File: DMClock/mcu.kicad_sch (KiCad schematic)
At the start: 31 parts, among them J7 Conn_01x02_Pin, J9 Conn_01x02_Pin, Q1 2SC1815, Q2 2SC1815, SW1 SW_Push, SW10 SW_Push, SW3 SW_SP3T (mode select), SW7 SW_Push, SW8 SW_Push, SW9 SW_Push, U1 PIC16F18346-P, U2 DS3231SN_

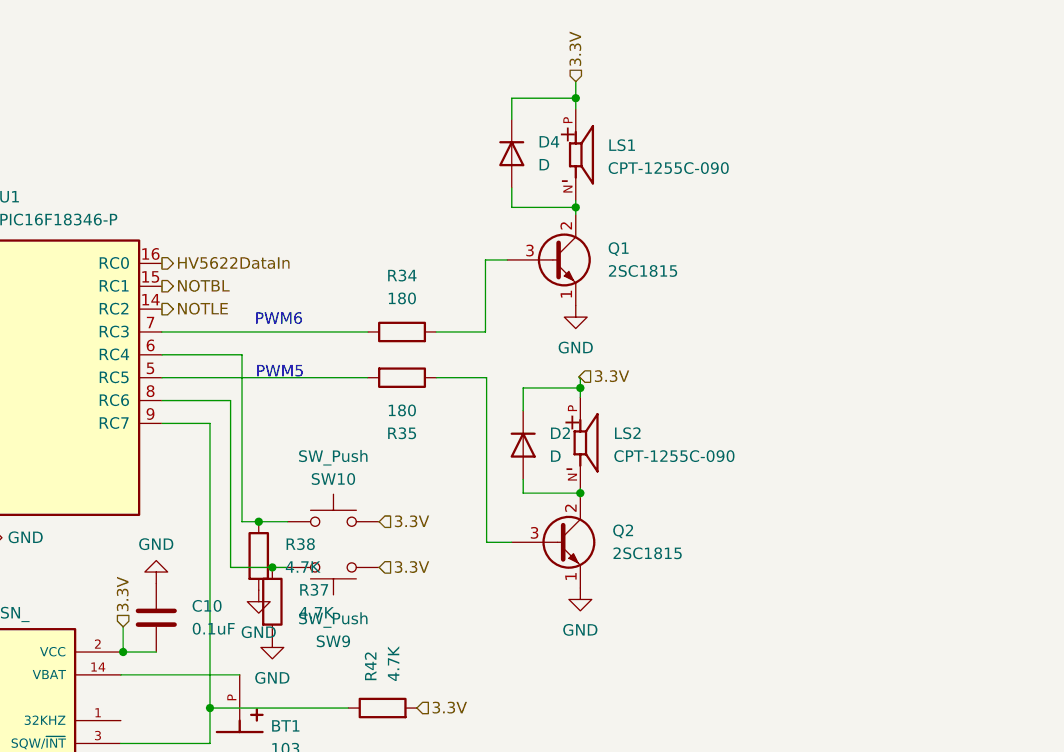
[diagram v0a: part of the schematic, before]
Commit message: need to add timer6 implementation
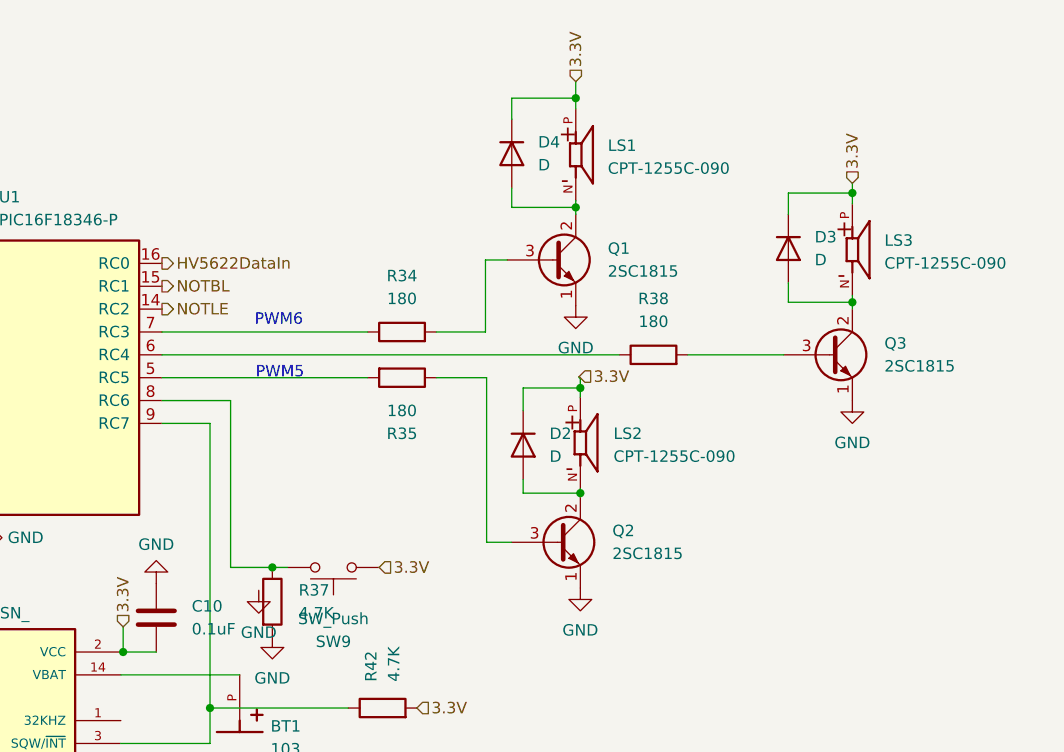
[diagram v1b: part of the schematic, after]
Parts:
- removed SW10: SW_Push, Connector_PinHeader_2.54mm:PinHeader_1x02_P2.54mm_Vertical, symbol Switch:SW_Push
- added D3: D, Diode_THT:D_A-405_P2.54mm_Vertical_AnodeUp, symbol Device:D
- added LS3: CPT-1255C-090, Footprints:CUI_CPT-1255C-090, symbol CPT-1255C-090:CPT-1255C-090
- added Q3: 2SC1815, Package_TO_SOT_THT:TO-92_Inline, symbol Transistor_BJT:2SC1815
- R38: value 4.7K -> 180
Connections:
- net 3.3V: now also D3.1 (K), LS3.P
- net GND: now also Q3.1 (E); no longer R38.2
- new net: D3.2 (A), LS3.N, Q3.2 (C)
- new net: Q3.3 (B), R38.2

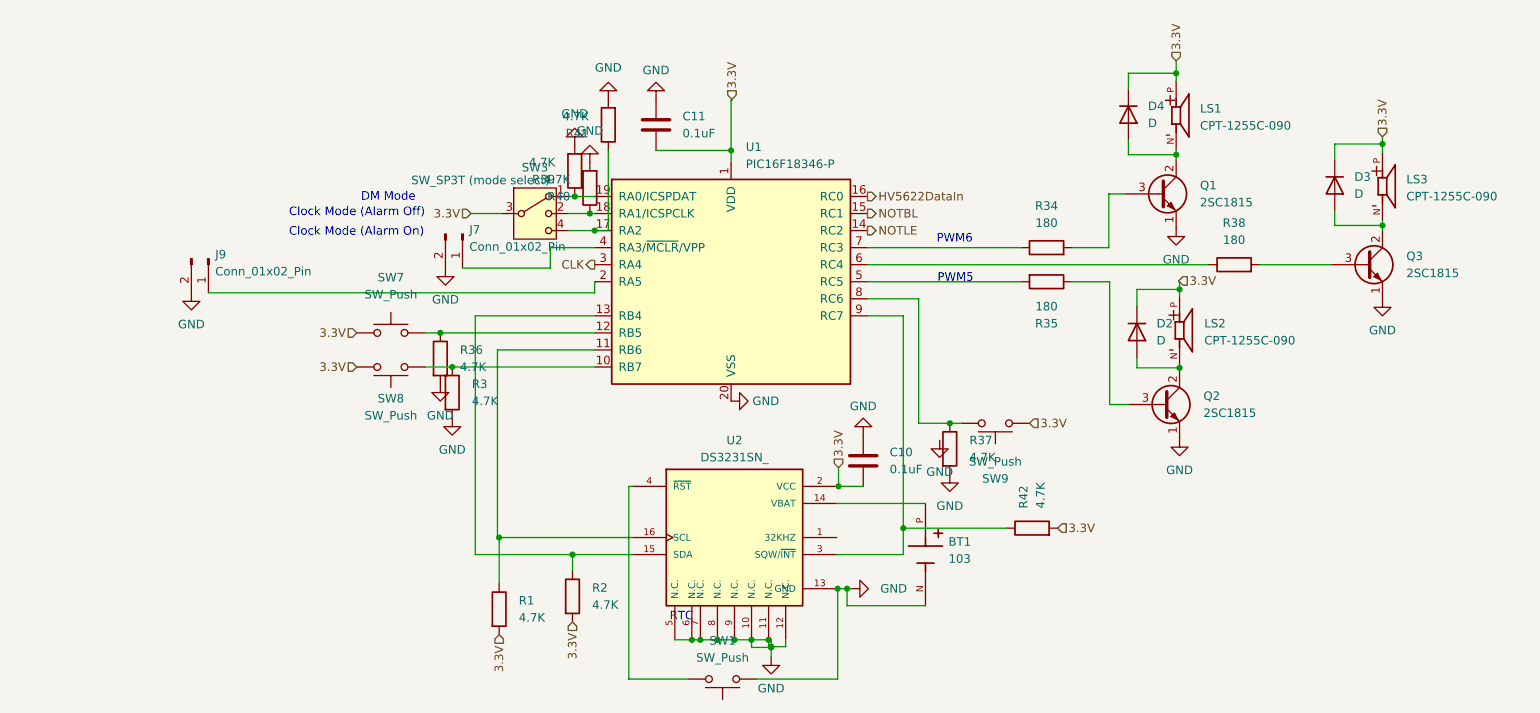
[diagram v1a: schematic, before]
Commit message: updated buck converter
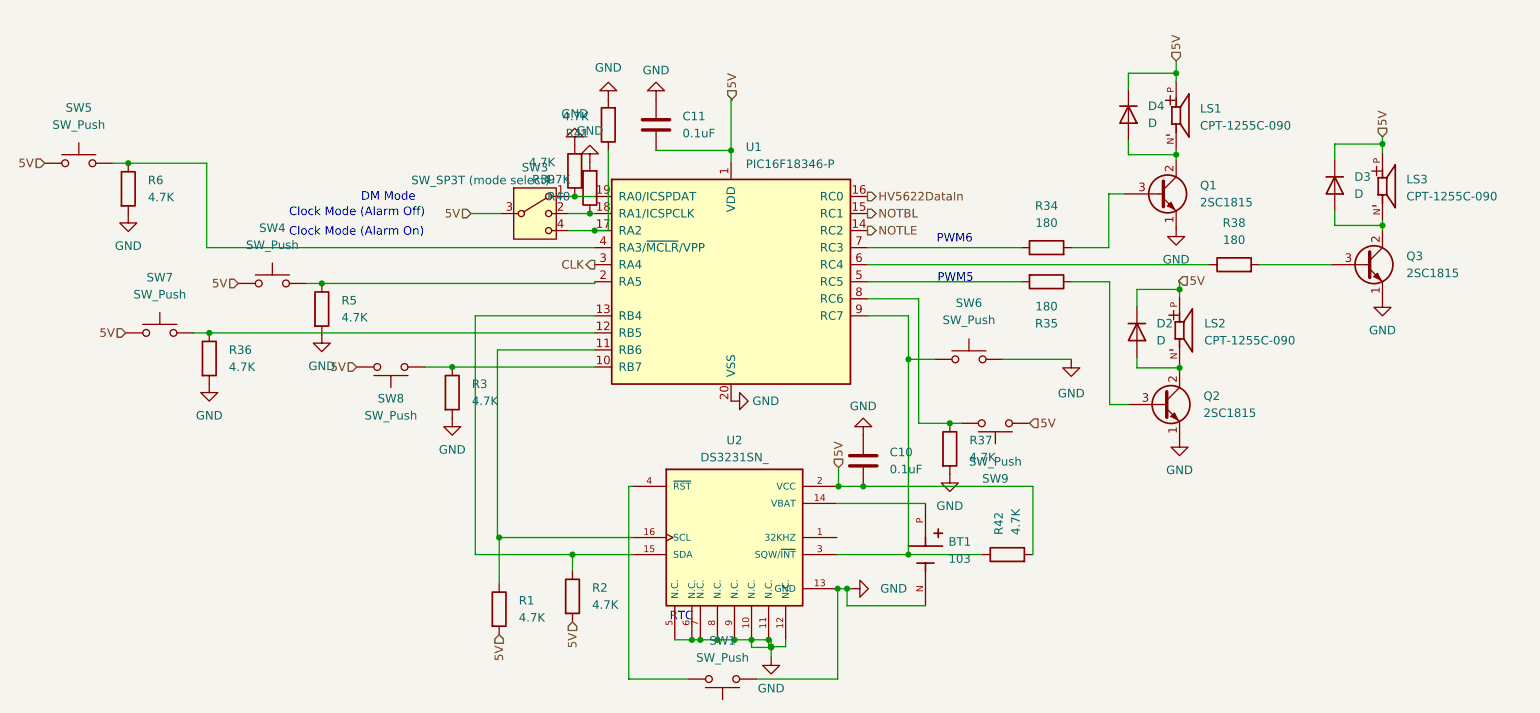
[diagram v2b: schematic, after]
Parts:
- removed J7, J9: Conn_01x02_Pin, Connector_PinSocket_2.54mm:PinSocket_1x02_P2.54mm_Vertical, symbol Connector:Conn_01x02_Pin
- added R5, R6: 4.7K, Resistor_THT:R_Axial_DIN0204_L3.6mm_D1.6mm_P2.54mm_Vertical, symbol Device:R
- added SW4, SW5, SW6: SW_Push, Connector_PinHeader_2.54mm:PinHeader_1x02_P2.54mm_Vertical, symbol Switch:SW_Push
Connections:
- net GND: now also R5.2, R6.2, SW6.2
- net at R42.1, U1.9 (RC7), U2.3 (SQW/~{INT}): now also SW6.1
- net at U1.2 (RA5): now also R5.1, SW4.2
- net at U1.4 (RA3/~{MCLR}/VPP): now also R6.1, SW5.2
- net 3.3V renamed 5V
- net 5V: now also SW4.1, SW5.1
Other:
- moved on the sheet: R36, R42, SW7
